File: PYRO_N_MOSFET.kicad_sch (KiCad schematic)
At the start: 14 parts, among them J2 Screw_Terminal, J6 Screw_Terminal, Q1 AO3400A, Q2_32mW1 AO3400A, Q4 AO3400A

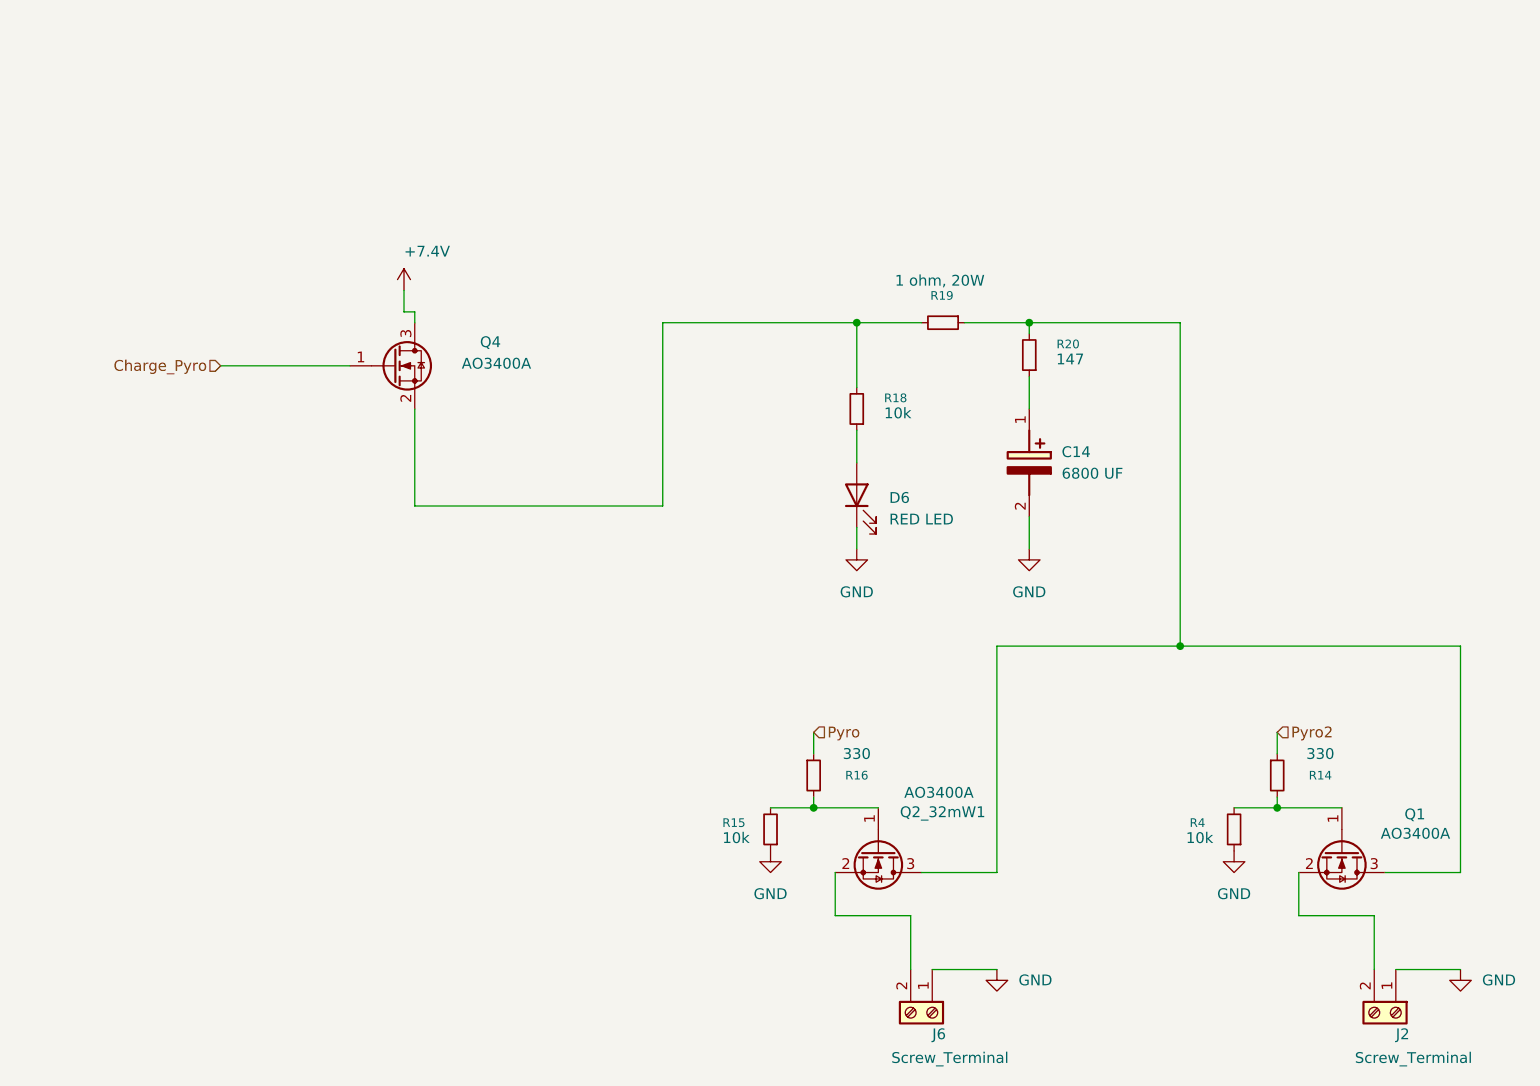
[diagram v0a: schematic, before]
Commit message: update Schematic
Fixed N channel mosfet pyros and set to low side trigger
removed unneeded 5v buck converter
rerouted/optmized gpio pins
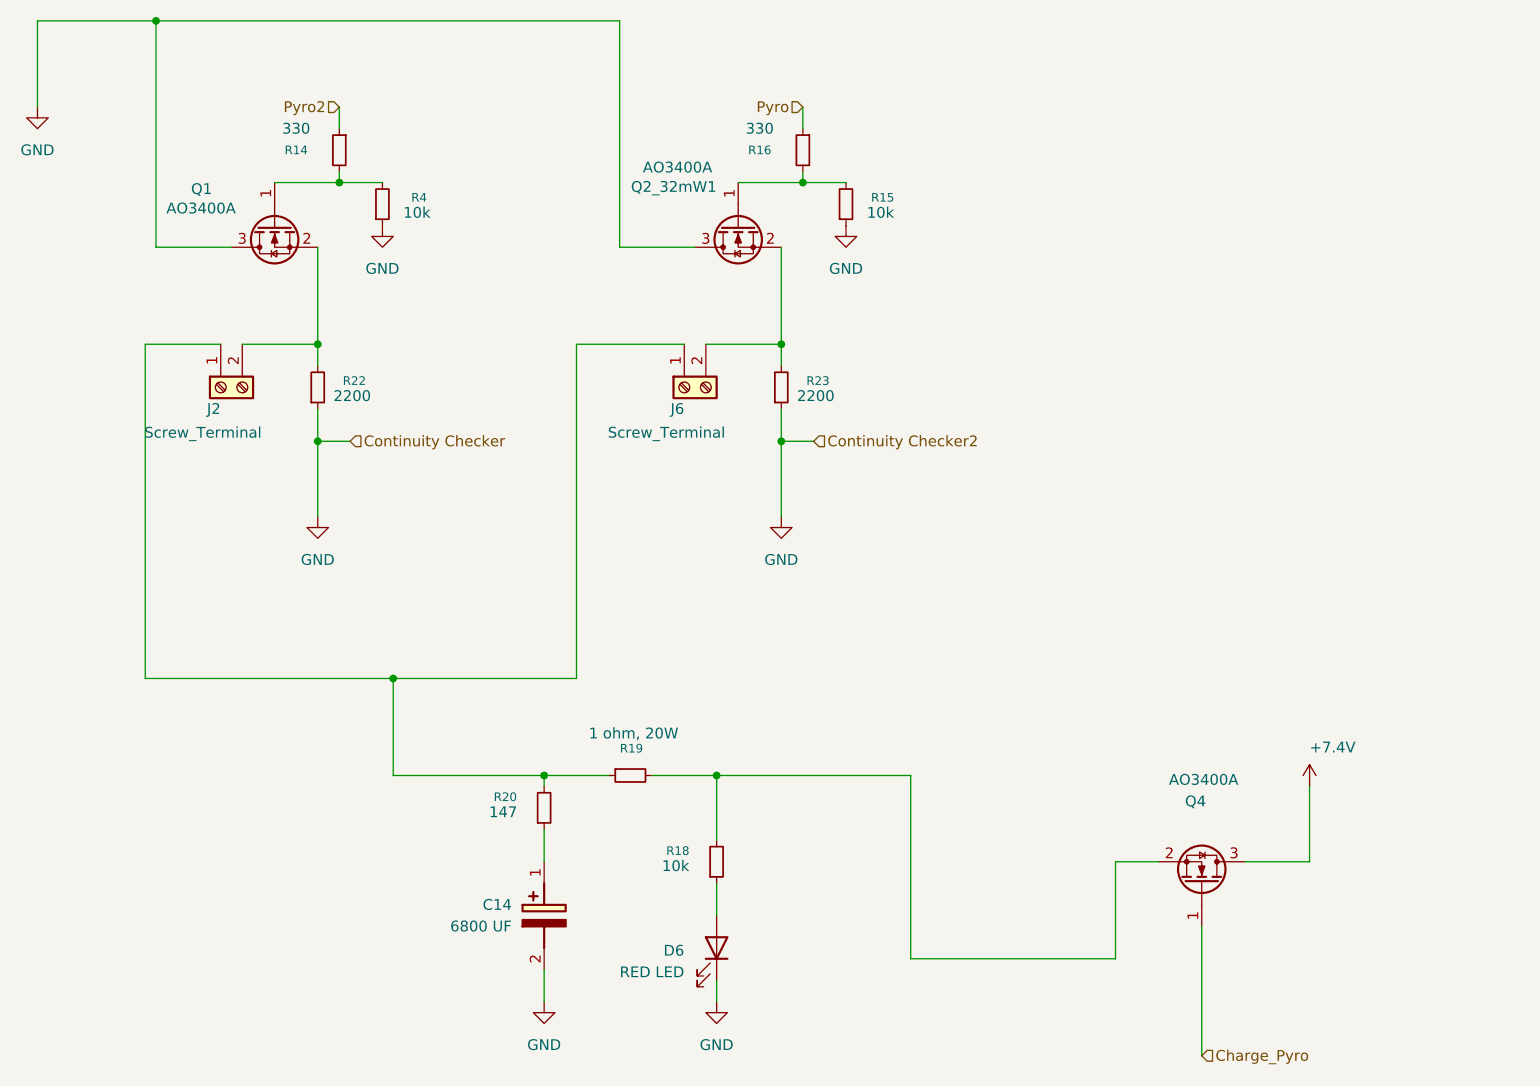
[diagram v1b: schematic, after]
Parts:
- added R22, R23: 2200, Resistor:R0402, symbol Device:R_Small
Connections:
- net GND: now also Q1.3 (D), Q2_32mW1.3 (D), R22.1, R23.1; no longer J2.1 (Pin_1), J6.1 (Pin_1)
- net at J2.2 (Pin_2), Q1.2 (S): now also R22.2
- net at R19.1, R20.2: now also J2.1 (Pin_1), J6.1 (Pin_1); no longer Q1.3 (D), Q2_32mW1.3 (D)
- net at J6.2 (Pin_2), Q2_32mW1.2 (S): now also R23.2
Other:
- moved on the sheet: C14, D6, J2, J6, Q1, Q2_32mW1, Q4, R14, R15, R16, R18, R19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
